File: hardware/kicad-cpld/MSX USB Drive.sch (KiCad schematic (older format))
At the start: 9 parts, among them J1 AVR-JTAG-10, J2 Conn_02x08_Odd_Even, U1 EPM7032_7064, U5 SST39SF040

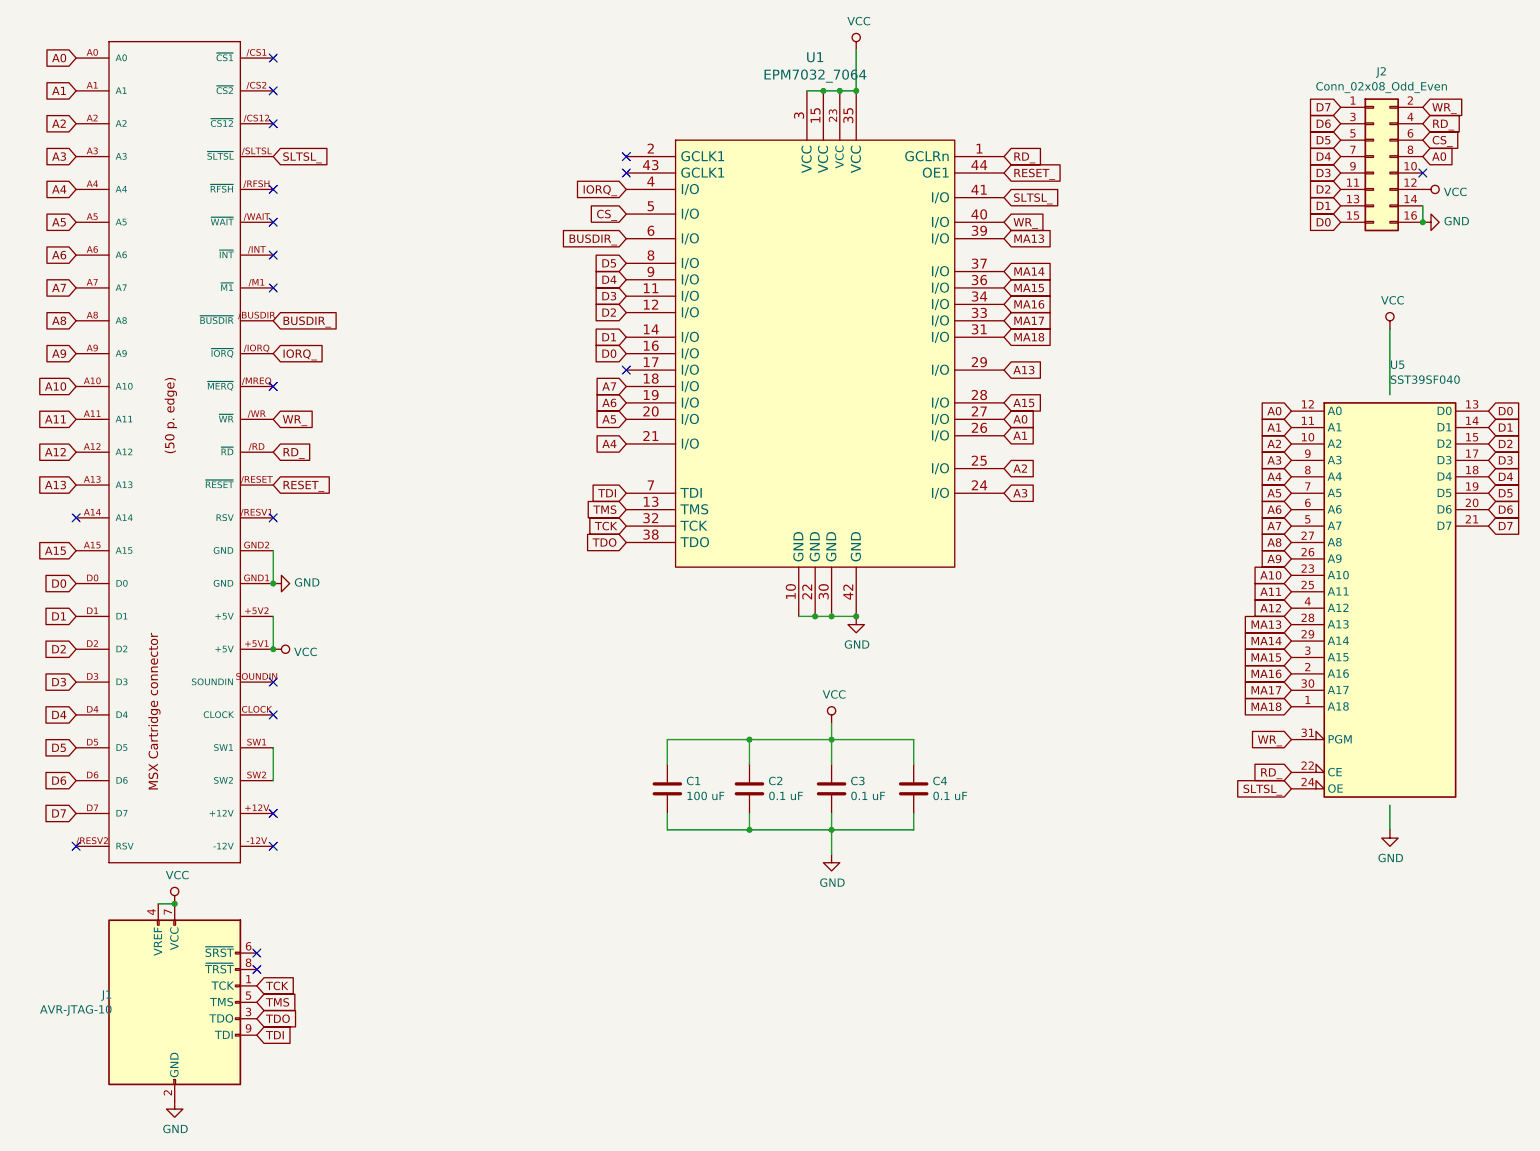
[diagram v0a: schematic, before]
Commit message: CPLD PCB Verilog + Flash software works
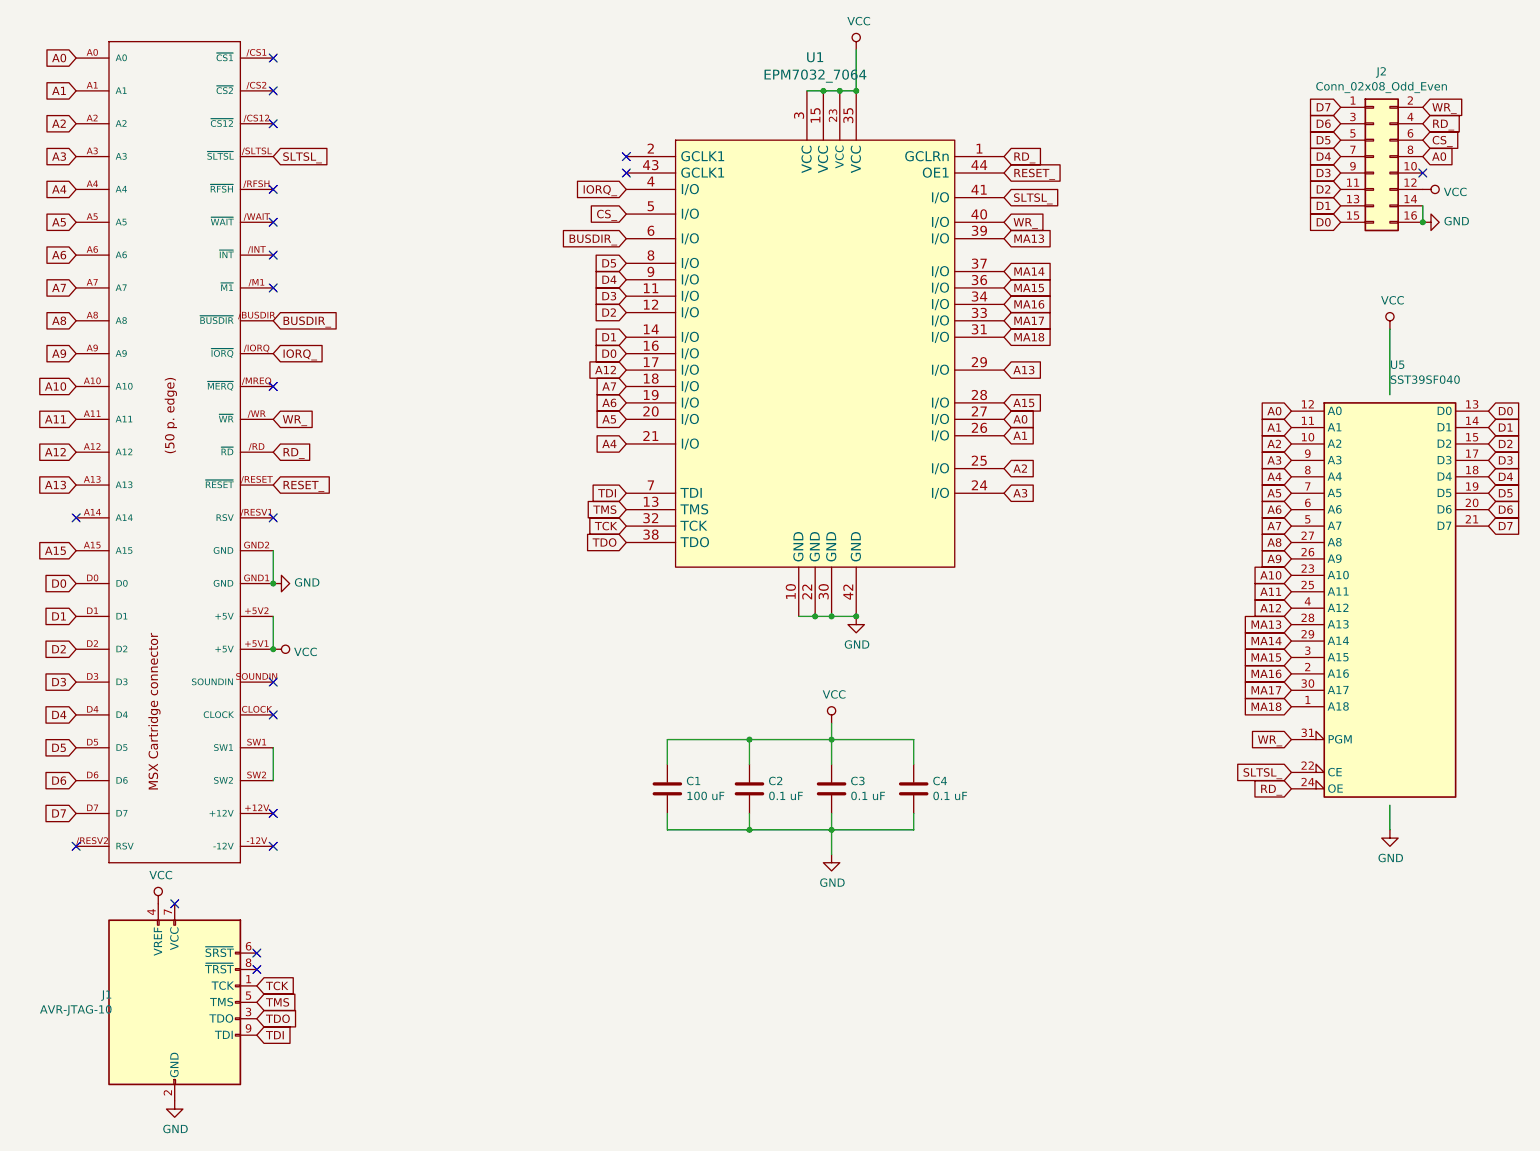
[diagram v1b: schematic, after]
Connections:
- net A12: now also U1.17 (I/O)
- net RD_: now also U5.24 (OE); no longer U5.22 (CE)
- net SLTSL_: now also U5.22 (CE); no longer U5.24 (OE)
- net VCC: no longer J1.7 (VCC)
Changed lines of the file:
@@
 Wire Wire Line
 	9100 3200 9100 2800
+Text GLabel 8500 5500 0    50   Input ~ 0
+SLTSL_
 Text GLabel 8500 5600 0    50   Input ~ 0
-SLTSL_
-Text GLabel 8500 5500 0    50   Input ~ 0
 RD_
 Text GLabel 8500 5300 0    50   Input ~ 0
@@
 F 3 "" H 5600 2950 60  0000 C CNN
 	1    5600 2950
-	1    0    0    -1
-$EndComp
-$Comp
-L Connector:AVR-JTAG-10 J1
-U 1 1 5E822CA8
-P 1700 6900
-F 0 "J1" H 1320 6946 50  0000 R CNN
-F 1 "AVR-JTAG-10" H 1320 6855 50  0000 R CNN
-F 2 "msx-usb-kicad-cpld:PinHeader_2x05_P2.54mm_Vertical" V 1550 7050 50  0001 C CNN
-F 3 " ~" H 425 6350 50  0001 C CNN
-	1    1700 6900
 	1    0    0    -1
 $EndComp
@@
 Text GLabel 8500 5100 0    50   Input ~ 0
 MA18
-Wire Wire Line
-	1600 6300 1700 6300
-$Comp
-L power:VCC #PWR0101
-U 1 1 5E8479A5
-P 1700 6300
-F 0 "#PWR0101" H 1700 6150 50  0001 C CNN
-F 1 "VCC" H 1717 6473 50  0000 C CNN
-F 2 "" H 1700 6300 50  0001 C CNN
-F 3 "" H 1700 6300 50  0001 C CNN
-	1    1700 6300
-	1    0    0    -1
-$EndComp
-Connection ~ 1700 6300
 $Comp
 L power:GND #PWR0102
@@
 NoConn ~ 4450 1750
 NoConn ~ 4450 1850
-NoConn ~ 4450 3050
+$Comp
+L Connector:AVR-JTAG-10 J1
+U 1 1 5E822CA8
+P 1700 6900
+F 0 "J1" H 1320 6946 50  0000 R CNN
+F 1 "AVR-JTAG-10" H 1320 6855 50  0000 R CNN
+F 2 "msx-usb-kicad-cpld:PinHeader_2x05_P2.54mm_Vertical" V 1550 7050 50  0001 C CNN
+F 3 " ~" H 425 6350 50  0001 C CNN
+	1    1700 6900
+	1    0    0    -1
+$EndComp
+$Comp
+L power:VCC #PWR0101
+U 1 1 5E8479A5
+P 1600 6300
+F 0 "#PWR0101" H 1600 6150 50  0001 C CNN
+F 1 "VCC" H 1617 6473 50  0000 C CNN
+F 2 "" H 1600 6300 50  0001 C CNN
+F 3 "" H 1600 6300 50  0001 C CNN
+	1    1600 6300
+	1    0    0    -1
+$EndComp
+NoConn ~ 1700 6300
+Text GLabel 4450 3050 0    50   Input ~ 0
+A12
 $EndSCHEMATC

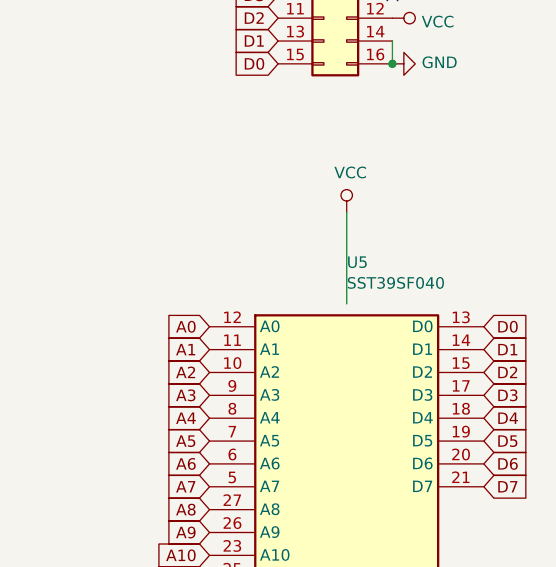
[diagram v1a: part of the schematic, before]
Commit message: Discrete PCB discontinued, flash changed AM29F040
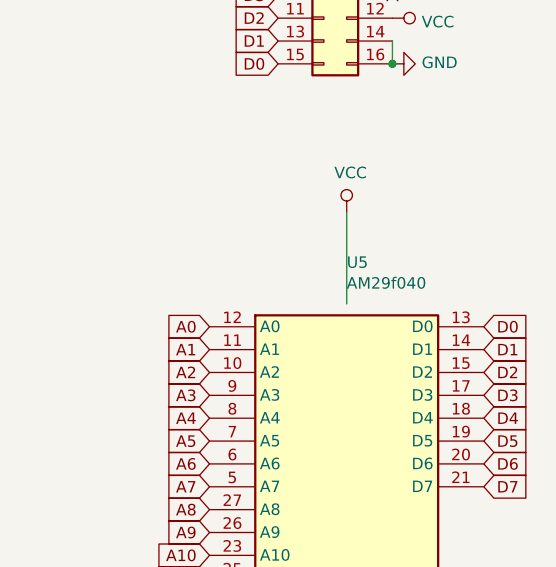
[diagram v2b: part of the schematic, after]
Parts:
- U5: value SST39SF040 -> AM29f040
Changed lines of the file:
@@
 P 9100 4500
 F 0 "U5" H 9100 5981 50  0000 L CNN
-F 1 "SST39SF040" H 9100 5890 50  0000 L CNN
+F 1 "AM29f040" H 9100 5890 50  0000 L CNN
 F 2 "msx-usb-kicad-cpld:DIP-32_W15.24mm_Socket" H 9100 4800 50  0001 C CNN
 F 3 "http://ww1.microchip.com/downloads/en/DeviceDoc/25022B.pdf" H 9100 4800 50  0001 C CNN
